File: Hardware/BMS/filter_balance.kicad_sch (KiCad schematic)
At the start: 7 parts

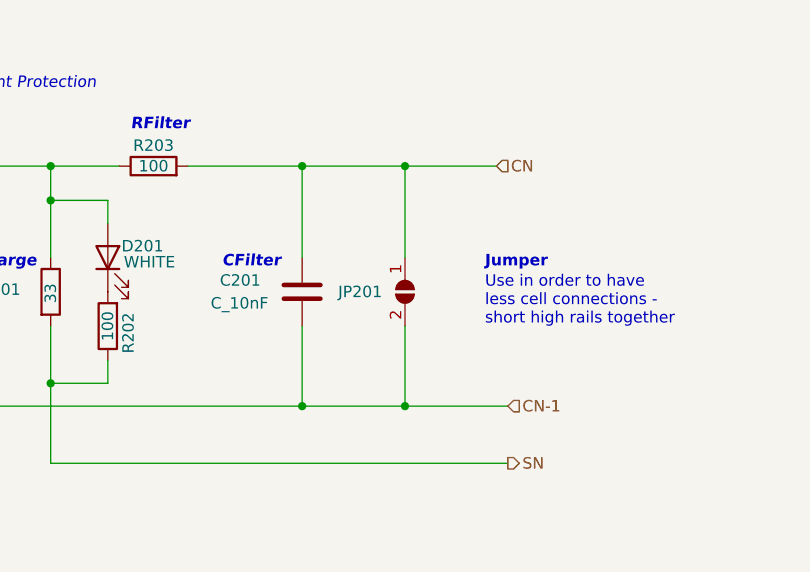
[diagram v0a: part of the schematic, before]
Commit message: BMS updates, power/fet final updates
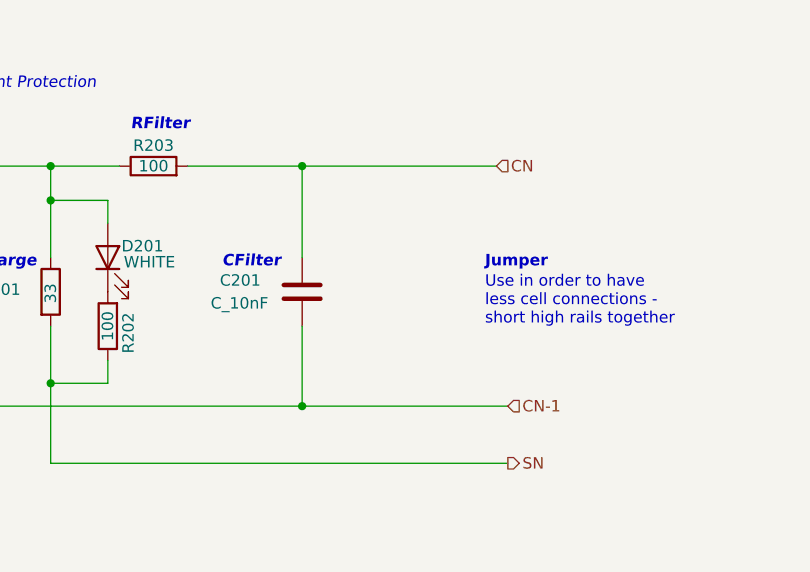
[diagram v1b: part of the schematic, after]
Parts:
- removed JP201: SolderJumper_2_Open, Jumper:SolderJumper-2_P1.3mm_Open_TrianglePad1.0x1.5mm, symbol Jumper:SolderJumper_2_Open
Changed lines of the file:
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@@
-	)
-	(junction
-		(at 182.88 76.2)
-		(diameter 0)
-		(color 0 0 0 0)
 	)
 	(junction
@@
 	)
 	(junction
-		(at 182.88 102.87)
-		(diameter 0)
-		(color 0 0 0 0)
-	)
-	(junction
 		(at 143.51 100.33)
 		(diameter 0)
@@
 	(wire
 		(pts
-			(xy 182.88 76.2) (xy 193.04 76.2)
+			(xy 171.45 76.2) (xy 193.04 76.2)
 		)
 		(stroke
@@
 	(wire
 		(pts
-			(xy 182.88 76.2) (xy 182.88 86.36)
-		)
-		(stroke
-			(width 0)
-			(type default)
-		)
-	)
-	(wire
-		(pts
 			(xy 109.22 102.87) (xy 171.45 102.87)
 		)
@@
 	(wire
 		(pts
-			(xy 171.45 76.2) (xy 182.88 76.2)
-		)
-		(stroke
-			(width 0)
-			(type default)
-		)
-	)
-	(wire
-		(pts
 			(xy 137.16 76.2) (xy 143.51 76.2)
 		)
@@
 	(wire
 		(pts
-			(xy 171.45 102.87) (xy 182.88 102.87)
+			(xy 171.45 102.87) (xy 194.31 102.87)
 		)
 		(stroke
@@
 		(pts
 			(xy 171.45 76.2) (xy 171.45 86.36)
-		)
-		(stroke
-			(width 0)
-			(type default)
-		)
-	)
-	(wire
-		(pts
-			(xy 182.88 102.87) (xy 194.31 102.87)
-		)
-		(stroke
-			(width 0)
-			(type default)
-		)
-	)
-	(wire
-		(pts
-			(xy 182.88 93.98) (xy 182.88 102.87)
 		)
 		(stroke
@@
 					(unit 1)
 				)
-			)
-		)
-	)
-	(symbol
-		(lib_id "Jumper:SolderJumper_2_Open")
-		(at 182.88 90.17 270)
-		(unit 1)
-		(exclude_from_sim no)
-		(in_bom no)
-		(on_board yes)
-		(dnp no)
-		(property "Reference" "JP201"
-			(at 180.34 90.17 90)
-			(effects
-				(font
-					(size 1.27 1.27)
-				)
-				(justify right)
-			)
-		)
-		(property "Value" "SolderJumper_2_Open"
-			(at 180.34 100.33 0)
-			(effects
-				(font
-					(size 1.27 1.27)
-				)
-				(justify right)
-				(hide yes)
-			)
-		)
-		(property "Footprint" "Jumper:SolderJumper-2_P1.3mm_Open_TrianglePad1.0x1.5mm"
-			(at 182.88 90.17 0)
-			(effects
-				(font
-					(size 1.27 1.27)
-				)
-				(hide yes)
-			)
-		)
-		(property "Datasheet" "~"
-			(at 182.88 90.17 0)
-			(effects
-				(font
-					(size 1.27 1.27)
-				)
-				(hide yes)
-			)
-		)
-		(property "Description" ""
-			(at 182.88 90.17 0)
-			(effects
-				(font
-					(size 1.27 1.27)
-				)
-				(hide yes)
-			)
-		)
-		(pin "1"
-		)
-		(pin "2"
-		)
-		(instances
-			(project "bms"
-				(path "/36848c1b-92a5-46b0-877b-0db2387c679c/826e6c70-848d-4f04-803e-a5eb891d5409/08939dd6-8002-48a6-bc3c-6d57039b8cb1"
-					(reference "JP1801")
-					(unit 1)
-				)
-				(path "/36848c1b-92a5-46b0-877b-0db2387c679c/826e6c70-848d-4f04-803e-a5eb891d5409/1776b018-8c42-4ffc-935d-22158017bf2f"
-					(reference "JP2101")
-					(unit 1)
-				)
-				(path "/36848c1b-92a5-46b0-877b-0db2387c679c/826e6c70-848d-4f04-803e-a5eb891d5409/19704c5a-78bc-41aa-be36-2f34e0d106cb"
-					(reference "JP1301")
-					(unit 1)
-				)
-				(path "/36848c1b-92a5-46b0-877b-0db2387c679c/826e6c70-848d-4f04-803e-a5eb891d5409/291371aa-8f00-485b-b59d-3c659613fdef"
-					(reference "JP701")
-					(unit 1)
-				)
-				(path "/36848c1b-92a5-46b0-877b-0db2387c679c/826e6c70-848d-4f04-803e-a5eb891d5409/2f3b7f9d-db27-4f04-af44-e56cb2c38fbc"
-					(reference "JP1701")
-					(unit 1)
-				)
-				(path "/36848c1b-92a5-46b0-877b-0db2387c679c/826e6c70-848d-4f04-803e-a5eb891d5409/66a2c798-220f-466d-a17c-351810975fec"
-					(reference "JP1901")
-					(unit 1)
-				)
-				(path "/36848c1b-92a5-46b0-877b-0db2387c679c/826e6c70-848d-4f04-803e-a5eb891d5409/85847120-5e6c-4155-8ac2-747adc018505"
-					(reference "JP2201")
-					(unit 1)
-				)
-				(path "/36848c1b-92a5-46b0-877b-0db2387c679c/826e6c70-848d-4f04-803e-a5eb891d5409/9e9ff205-786a-4005-8122-23a4d17d9d4f"
-					(reference "JP1501")
-					(unit 1)
-				)
-				(path "/36848c1b-92a5-46b0-877b-0db2387c679c/826e6c70-848d-4f04-803e-a5eb891d5409/aaf9f96a-7ddf-4995-af3f-f87e14c8af2d"
-					(reference "JP1401")
-					(unit 1)
-				)
-				(path "/36848c1b-92a5-46b0-877b-0db2387c679c/826e6c70-848d-4f04-803e-a5eb891d5409/c9e0032d-4014-4eee-89ce-a01f9e17c7e7"
-					(reference "JP1201")
-					(unit 1)
-				)
-				(path "/36848c1b-92a5-46b0-877b-0db2387c679c/826e6c70-848d-4f04-803e-a5eb891d5409/cca58e24-f26b-4a68-933b-39fd7594f2b8"
-					(reference "JP2001")
-					(unit 1)
-				)
-				(path "/36848c1b-92a5-46b0-877b-0db2387c679c/826e6c70-848d-4f04-803e-a5eb891d5409/d2d0499b-0d0c-497e-b229-513cca94df20"
-					(reference "JP1601")
-					(unit 1)
-				)
-				(path "/36848c1b-92a5-46b0-877b-0db2387c679c/826e6c70-848d-4f04-803e-a5eb891d5409/d46111bc-cccb-419c-90ce-3d65698ee648"
-					(reference "JP1001")
-					(unit 1)
-				)
-				(path "/36848c1b-92a5-46b0-877b-0db2387c679c/826e6c70-848d-4f04-803e-a5eb891d5409/f9712816-d0d1-4731-9589-3dc1d67e51f8"
-					(reference "JP201")
-					(unit 1)
-				)

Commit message: bms gotten to 0 unrouted traces!
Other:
- note removed: "Cells: Samsung 40T 21700 https://cdn.shopify.com/s/files/1/0481/9678/0183/files/Samsung_Introduction_of_New_40T_v3.pdf?v=1612843210"
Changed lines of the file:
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@@
-		)
-	)
-	(text "Cells: Samsung 40T 21700\nhttps://cdn.shopify.com/s/files/1/0481/9678/0183/files/Samsung_Introduction_of_New_40T_v3.pdf?v=1612843210"
-		(exclude_from_sim no)
-		(at 29.21 194.31 0)
-		(effects
-			(font
-				(size 1.27 1.27)
-				(italic yes)
-			)
-			(justify left bottom)
 		)
 	)
